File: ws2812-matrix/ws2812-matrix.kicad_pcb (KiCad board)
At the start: 2 copper layers, 80 x 80 mm, 268 parts, among them J1 Conn_01x03, J2 Conn_01x03

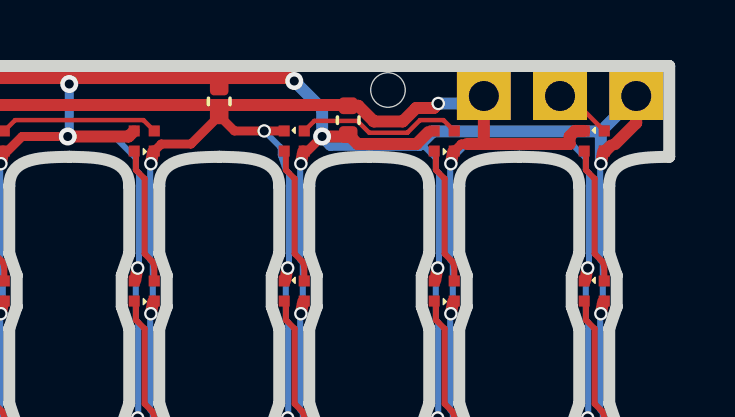
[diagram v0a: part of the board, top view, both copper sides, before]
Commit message: ws2812-matrix: gnd not via bottom layer
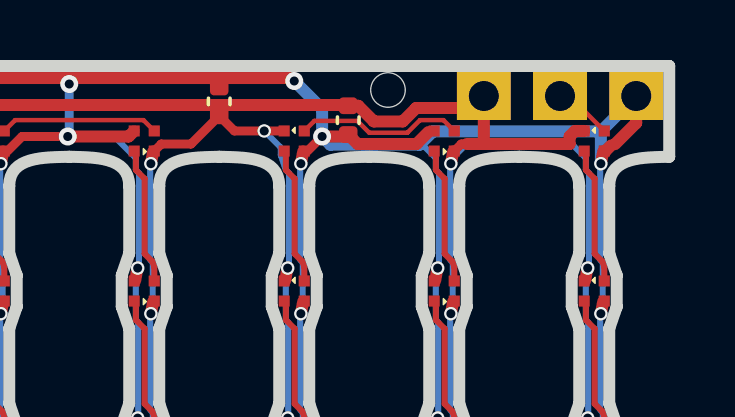
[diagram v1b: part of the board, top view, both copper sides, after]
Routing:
- net GND: vias 256 -> 255
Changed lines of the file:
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@@
 	)
 	(segment
-		(start 117.132516 48.825)
-		(end 117.655516 49.348)
-		(width 0.4)
-		(layer "F.Cu")
-		(net 3)
-	)
-	(segment
 		(start 54.565 49.665)
 		(end 53.68 48.78)
@@
 	)
 	(segment
-		(start 118.616512 49.348)
-		(end 119.064512 48.9)
-		(width 0.4)
-		(layer "F.Cu")
-		(net 3)
-	)
-	(segment
-		(start 119.65 48.9)
-		(end 119.8 48.75)
-		(width 0.4)
-		(layer "F.Cu")
-		(net 3)
-	)
-	(segment
 		(start 92.5 49.16)
 		(end 91.559 50.101)
@@
 	)
 	(segment
+		(start 119.064512 48.9)
+		(end 120.92 48.9)
+		(width 0.4)
+		(layer "F.Cu")
+		(net 3)
+	)
+	(segment
 		(start 64 49.665)
 		(end 63.005 49.665)
@@
 	)
 	(segment
-		(start 117.655516 49.348)
-		(end 118.616512 49.348)
+		(start 117.132516 48.825)
+		(end 117.655516 49.348)
 		(width 0.4)
 		(layer "F.Cu")
@@
 	)
 	(segment
+		(start 117.655516 49.348)
+		(end 118.616512 49.348)
+		(width 0.4)
+		(layer "F.Cu")
+		(net 3)
+	)
+	(segment
 		(start 74 49.665)
 		(end 73.005 49.665)
@@
 	)
 	(segment
+		(start 118.616512 49.348)
+		(end 119.064512 48.9)
+		(width 0.4)
+		(layer "F.Cu")
+		(net 3)
+	)
+	(segment
 		(start 124.363 49.665)
 		(end 124.665 49.665)
@@
 	)
 	(segment
-		(start 116.8 48.825)
-		(end 117.132516 48.825)
+		(start 120.92 48.9)
+		(end 121.32 48.5)
 		(width 0.4)
 		(layer "F.Cu")
@@
 	)
 	(segment
+		(start 116.8 48.825)
+		(end 117.132516 48.825)
+		(width 0.4)
+		(layer "F.Cu")
+		(net 3)
+	)
+	(segment
 		(start 122.7 50.1)
 		(end 121.2 50.1)
@@
 	)
 	(segment
-		(start 119.064512 48.9)
-		(end 119.65 48.9)
-		(width 0.4)
-		(layer "F.Cu")
-		(net 3)
-	)
-	(segment
 		(start 116.775 48.8)
 		(end 116.8 48.825)
@@
 		(net 3)
 	)
-	(via
-		(at 119.8 48.75)
-		(size 0.45)
-		(drill 0.3)
-		(layers "F.Cu" "B.Cu")
-		(net 3)
-	)
 	(segment
 		(start 50.282699 109.043166)
@@
 	)
 	(segment
-		(start 121.07 48.75)
-		(end 121.32 48.5)
-		(width 0.4)
-		(layer "B.Cu")
-		(net 3)
-	)
-	(segment
 		(start 74.801 84.217491)
 		(end 74.801 81.044066)
@@
 		(layer "B.Cu")
 		(net 3)
-	)
-	(segment
-		(start 119.8 48.75)
-		(end 121.07 48.75)
-		(width 0.4)
-		(layer "B.Cu")
-		(net 3)
